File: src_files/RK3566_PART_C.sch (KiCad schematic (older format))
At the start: 78 parts, among them J4 3-1734592-0, J5 3-1734592-0, J6 3-1734592-0, Q3 2SK3018, Q4 2SK3018, Q5 2SK3018, U1 RK3566, U10 ESD5304D-TP, U8 ESD5304D-TP, U9 ESD5304D-TP

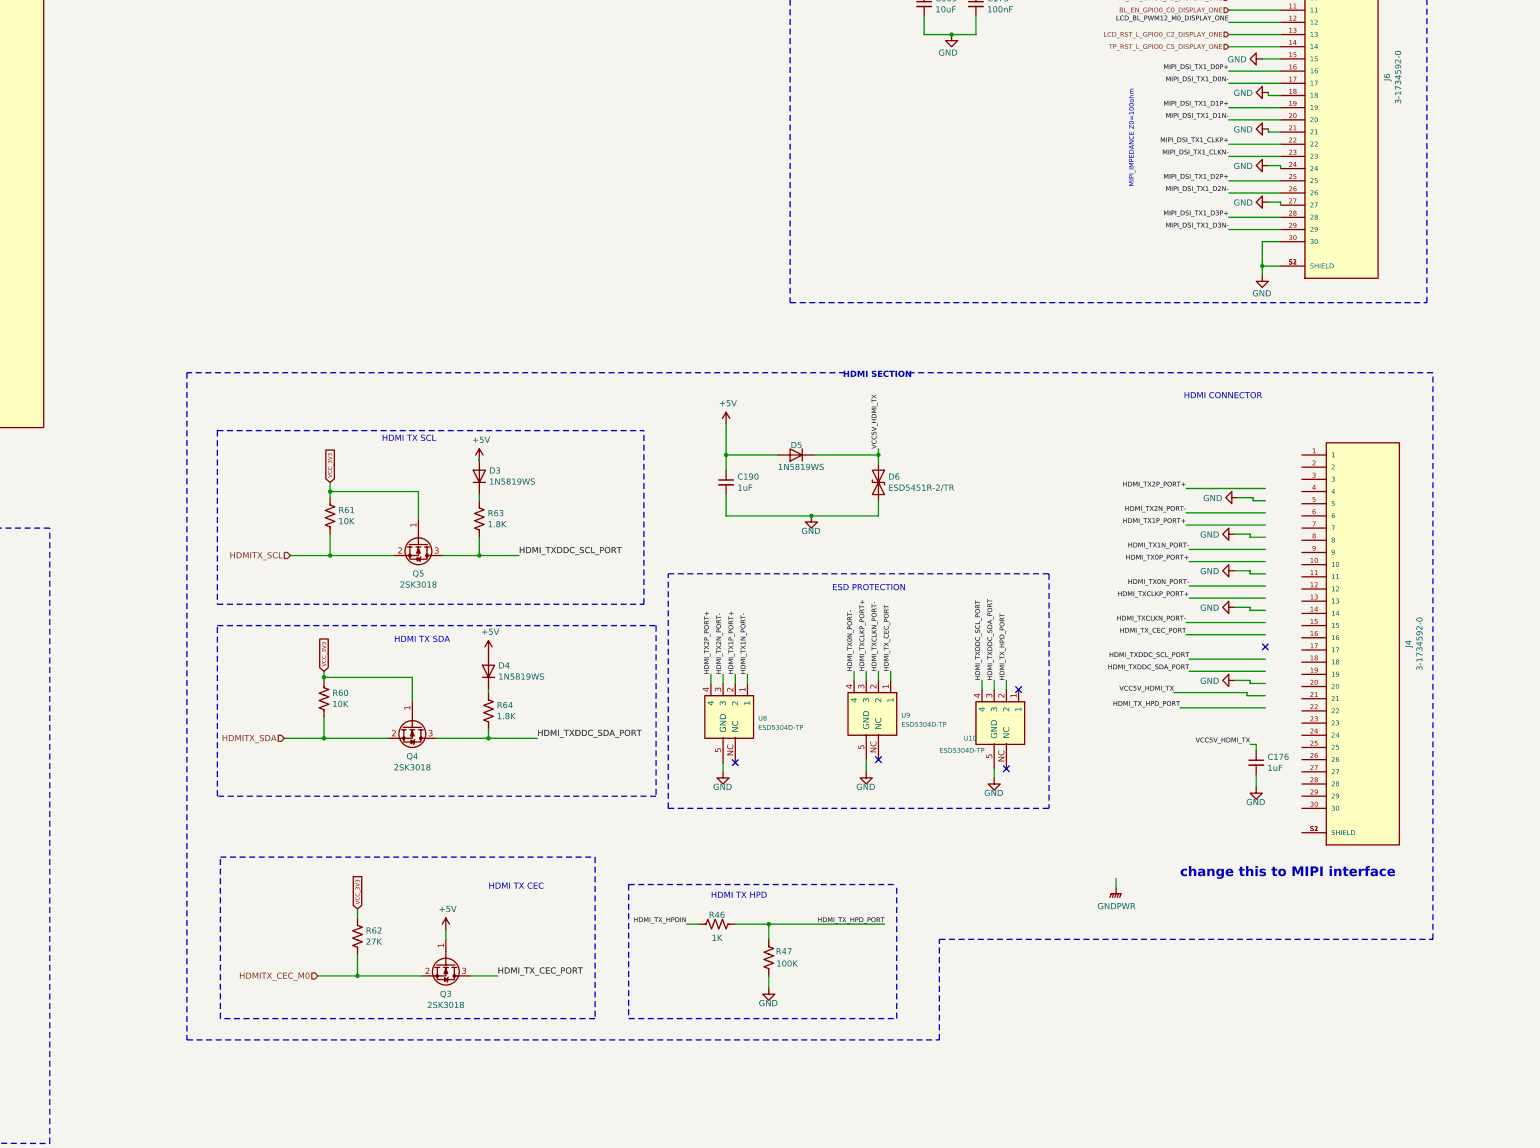
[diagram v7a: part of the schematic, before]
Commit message: update 1 extra hdmi to mipi interface
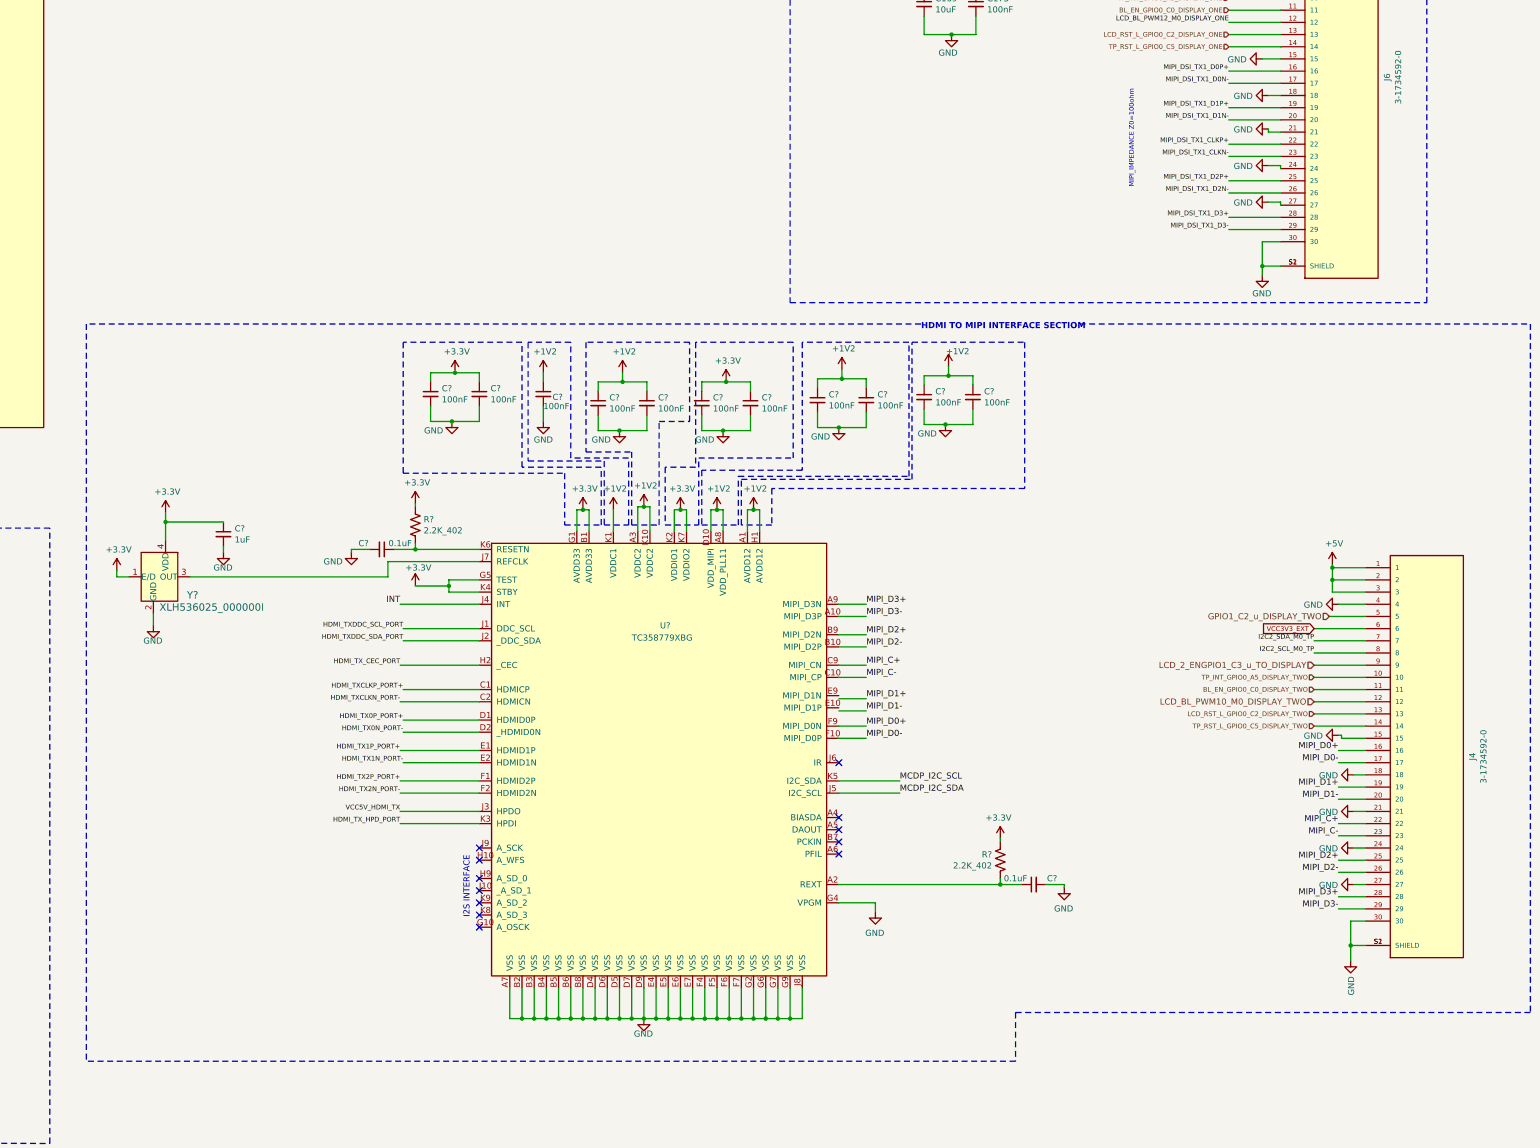
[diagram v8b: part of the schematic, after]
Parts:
- removed C176, C190: 1uF, Capacitor_SMD:C_0402_1005Metric, symbol Device:C_Small
- removed D3, D4, D5: 1N5819WS, Diode_SMD:D_SOD-323, symbol Device:D
- removed D6: ESD5451R-2/TR, greencharge-footprints:DFP1006-2L, symbol Device:D_TVS
- removed Q3, Q4, Q5: 2SK3018, digikey-footprints:SOT-23-3, symbol Device:Q_NMOS_GSD
- removed R46: 1K, Resistor_SMD:R_0402_1005Metric, symbol Device:R_US
- removed R47: 100K, Resistor_SMD:R_0402_1005Metric, symbol Device:R_US
- removed R60, R61: 10K, Resistor_SMD:R_0402_1005Metric, symbol Device:R_US
- removed R62: 27K, Resistor_SMD:R_0402_1005Metric, symbol Device:R_US
- removed R63, R64: 1.8K, Resistor_SMD:R_0402_1005Metric, symbol Device:R_US
- removed U10, U8, U9: ESD5304D-TP, greencharge-footprints:ESD5304D-TP, symbol GCL_Integrated-Circuits:ESD5304D-TP
- added C? (x2): 0.1uF, Capacitor_SMD:C_0402_1005Metric, symbol Device:C_Small
- added C?: 1uF, Capacitor_SMD:C_0402_1005Metric, symbol Device:C_Small
- added C? (x11): 100nF, Capacitor_SMD:C_0402_1005Metric, symbol Device:C_Small
- added R? (x2): 2.2K_402, Resistor_SMD:R_0402_1005Metric, symbol Device:R_US
- added U?: TC358779XBG, symbol GCL_Integrated-Circuits:TC358779XBG
- added Y?: XLH536025_000000I, Crystal:Crystal_SMD_EuroQuartz_MT-4Pin_3.2x2.5mm, symbol dk_Oscillators:XLH536025_000000I
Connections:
- net labels added: +1V2, +3.3V, BL_EN_GPIO0_C0_DISPLAY_TWO, GPIO1_C2_u_DISPLAY_TWO, INT, LCD_2_ENGPIO1_C3_u_TO_DISPLAY, LCD_BL_PWM10_M0_DISPLAY_TWO, LCD_RST_L_GPIO0_C2_DISPLAY_TWO, MIPI_C+, MIPI_C-, MIPI_D0+, MIPI_D0-, MIPI_D1+, MIPI_D1-, MIPI_D2+, MIPI_D2-, MIPI_D3+, MIPI_D3-, MIPI_DSI_TX1_D3+, MIPI_DSI_TX1_D3-, TP_INT_GPIO0_A5_DISPLAY_TWO, TP_RST_L_GPIO0_C5_DISPLAY_TWO
- net labels removed: GNDPWR, HDMITX_CEC_M0, HDMITX_SCL, HDMITX_SDA, VCC_3V3
- wire segments 386 -> 501
- no-connect marks 26 -> 33
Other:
- note added: "HDMI TO MIPI INTERFACE SECTIOM"
- note added: "I2S INTERFACE"
- note removed: "ESD PROTECTION"
- note removed: "HDMI CONNECTOR"
- note removed: "HDMI SECTION"
- note removed: "HDMI TX CEC"
- note removed: "HDMI TX HPD"
- note removed: "HDMI TX SCL\n"
- note removed: "HDMI TX SDA"
- note removed: "change this to MIPI interface"
- moved on the sheet: J4
